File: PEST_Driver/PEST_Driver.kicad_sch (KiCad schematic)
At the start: 12 parts, among them J9 Conn_01x09, U1 INA199xxDCK

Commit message: Added independent signal ground to schematic
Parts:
- removed J9: Conn_01x09, Connector_PinSocket_2.54mm:PinSocket_1x09_P2.54mm_Vertical, symbol Connector_Generic:Conn_01x09
- added J9: Conn_01x10, symbol Connector_Generic:Conn_01x10
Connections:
- net CLK: now also J9.7 (Pin_7)
- net GND: now also J9.1 (Pin_1); no longer R100.2, R98.2, R99.2, U1.1 (REF), U1.2 (GND)
- net PWM: now also J9.9 (Pin_9)
- net RCLK: now also J9.8 (Pin_8)
- net SERX: now also J9.5 (Pin_5)
- net SERY: now also J9.6 (Pin_6)
- net VCC: now also J9.4 (Pin_4)
- net VIN: now also J9.2 (Pin_2)
- net VOUT: now also J9.10 (Pin_10)
- new net GNDS: J9.3 (Pin_3), R100.2, R98.2, R99.2, U1.1 (REF), U1.2 (GND)
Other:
- moved on the sheet: C19

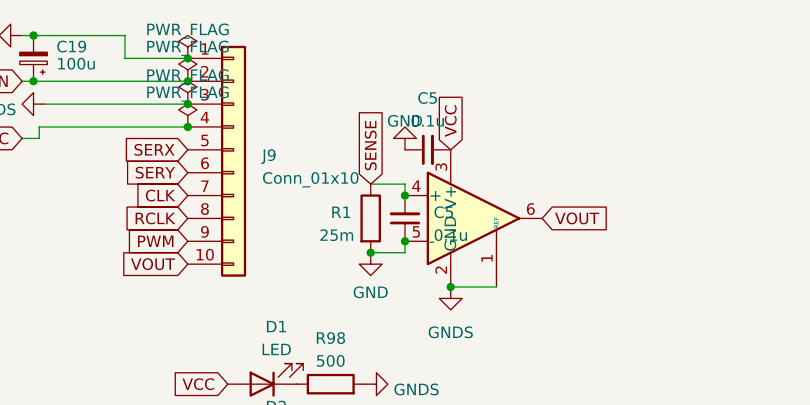
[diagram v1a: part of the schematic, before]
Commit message: Finished wiring independent MOSFET and logic grounds
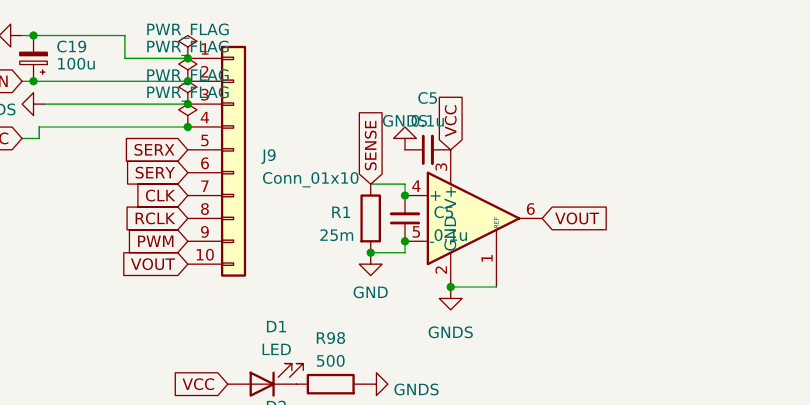
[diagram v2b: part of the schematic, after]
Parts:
- J9: footprint (none) -> Connector_PinSocket_2.54mm:PinSocket_1x10_P2.54mm_Vertical
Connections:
- net GND: no longer C5.1
- net GNDS: now also C5.1
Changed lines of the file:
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@@
-    )
-  )
-  (symbol (lib_id "power:GND") (at 60.325 28.575 180) (unit 1)
-    (in_bom yes) (on_board yes) (dnp no) (fields_autoplaced)
-    (property "Reference" "#PWR0126" (at 60.325 22.225 0)
-      (effects (font (size 1.27 1.27)) hide)
-    )
-    (property "Value" "GND" (at 60.325 25.4 0)
-      (effects (font (size 1.27 1.27)))
-    )
-    (property "Footprint" "" (at 60.325 28.575 0)
-      (effects (font (size 1.27 1.27)) hide)
-    )
-    (property "Datasheet" "" (at 60.325 28.575 0)
-      (effects (font (size 1.27 1.27)) hide)
-    )
-    (pin "1")
-    (instances
-      (project "PEST_Driver"
-        (path "/1312aa0a-e5d3-4b8d-ac4b-b6abdfb7d180/14e19459-9bf9-4345-8cad-a4f2aa65a7bc"
-          (reference "#PWR0126") (unit 1)
-        )
-        (path "/1312aa0a-e5d3-4b8d-ac4b-b6abdfb7d180"
-          (reference "#PWR0138") (unit 1)
-        )
-      )
     )
   )
@@
       (effects (font (size 1.27 1.27)) (justify left))
     )
-    (property "Footprint" "" (at 41.275 28.575 0)
+    (property "Footprint" "Connector_PinSocket_2.54mm:PinSocket_1x10_P2.54mm_Vertical" (at 41.275 28.575 0)
       (effects (font (size 1.27 1.27)) hide)
     )
@@
         )
       )
+    )
+  )
+  (symbol (lib_id "power:GNDS") (at 60.325 28.575 180) (unit 1)
+    (in_bom yes) (on_board yes) (dnp no) (fields_autoplaced)
+    (property "Reference" "#PWR078" (at 60.325 22.225 0)
+      (effects (font (size 1.27 1.27)) hide)
+    )
+    (property "Value" "GNDS" (at 60.325 25.4 0)
+      (effects (font (size 1.27 1.27)))
+    )
+    (property "Footprint" "" (at 60.325 28.575 0)
+      (effects (font (size 1.27 1.27)) hide)
+    )
+    (property "Datasheet" "" (at 60.325 28.575 0)
+      (effects (font (size 1.27 1.27)) hide)
+    )
+    (pin "1")
+    (instances
+      (project "PEST_Driver"
+        (path "/1312aa0a-e5d3-4b8d-ac4b-b6abdfb7d180"
+          (reference "#PWR078") (unit 1)
+        )
+      )

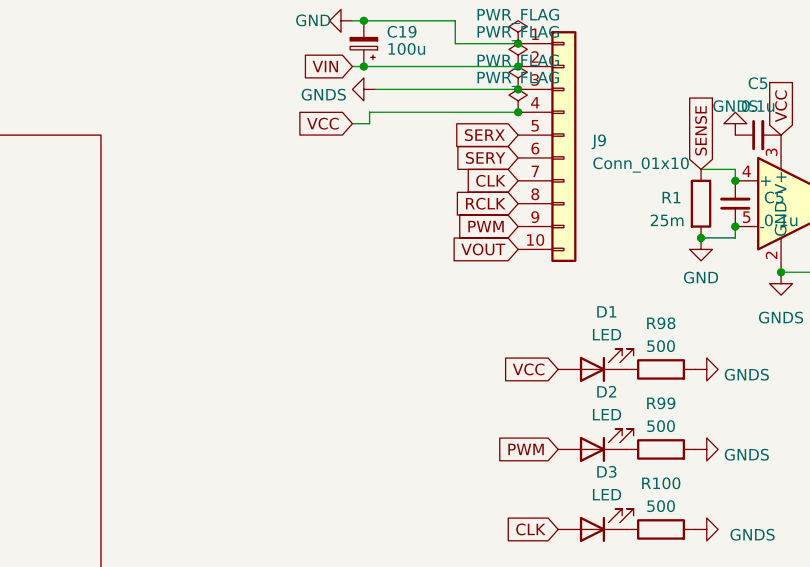
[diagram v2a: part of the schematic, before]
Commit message: Added more pulldown resistors to PEST Driver
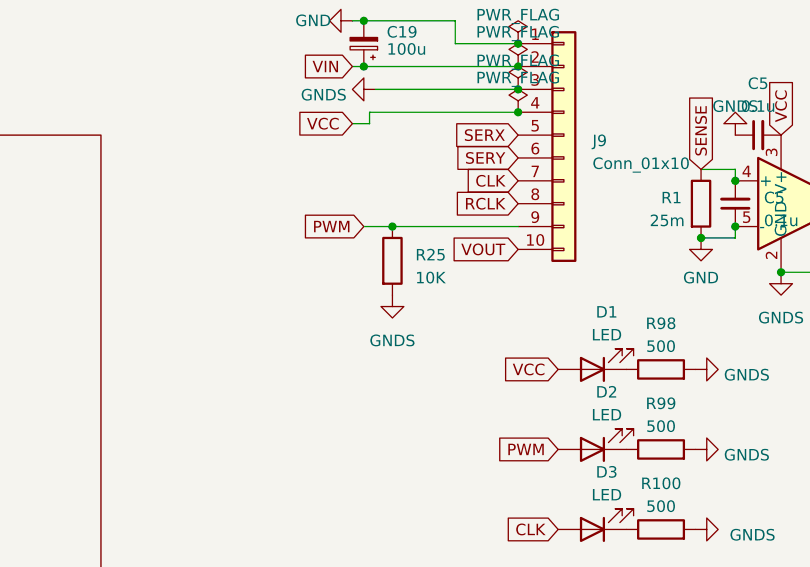
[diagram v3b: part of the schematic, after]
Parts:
- added R25: 10K, Resistor_SMD:R_0402_1005Metric, symbol Device:R
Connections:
- net GNDS: now also R25.2
- net PWM: now also R25.1
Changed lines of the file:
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@@
   (junction (at 56.515 40.005) (diameter 0) (color 0 0 0 0)
   )
+  (junction (at 22.225 38.735) (diameter 0) (color 0 0 0 0)
+  )
   (junction (at 60.325 33.655) (diameter 0) (color 0 0 0 0)
   )
@@
   (junction (at 19.05 15.875) (diameter 0) (color 0 0 0 0)
   )
+  (wire (pts (xy 22.225 38.735) (xy 36.195 38.735))
+    (stroke (width 0) (type default))
+  )
   (wire (pts (xy 65.405 43.815) (xy 70.485 43.815))
     (stroke (width 0) (type default))
@@
   )
   (wire (pts (xy 29.21 15.875) (xy 29.21 18.415))
+    (stroke (width 0) (type default))
+  )
+  (wire (pts (xy 19.05 38.735) (xy 22.225 38.735))
     (stroke (width 0) (type default))
   )
@@
     )
   )
-  (global_label "PWM" (shape input) (at 36.195 38.735 180) (fields_autoplaced)
-    (effects (font (size 1.27 1.27)) (justify right))
-    (property "Intersheetrefs" "${INTERSHEET_REFS}" (at 6.35 -6.35 0)
+  (global_label "PWM" (shape input) (at 19.05 38.735 180) (fields_autoplaced)
+    (effects (font (size 1.27 1.27)) (justify right))
+    (property "Intersheetrefs" "${INTERSHEET_REFS}" (at -10.795 -6.35 0)
       (effects (font (size 1.27 1.27)) hide)
     )
@@
     )
   )
+  (symbol (lib_id "Device:R") (at 22.225 42.545 0) (unit 1)
+    (in_bom yes) (on_board yes) (dnp no) (fields_autoplaced)
+    (property "Reference" "R25" (at 24.765 41.91 0)
+      (effects (font (size 1.27 1.27)) (justify left))
+    )
+    (property "Value" "10K" (at 24.765 44.45 0)
+      (effects (font (size 1.27 1.27)) (justify left))
+    )
+    (property "Footprint" "Resistor_SMD:R_0402_1005Metric" (at 20.447 42.545 90)
+      (effects (font (size 1.27 1.27)) hide)
+    )
+    (property "Datasheet" "~" (at 22.225 42.545 0)
+      (effects (font (size 1.27 1.27)) hide)
+    )
+    (pin "1")
+    (pin "2")
+    (instances
+      (project "PEST_Driver"
+        (path "/1312aa0a-e5d3-4b8d-ac4b-b6abdfb7d180/5f0c4818-2843-4085-a63a-fb9643216ecf"
+          (reference "R25") (unit 1)
+        )
+        (path "/1312aa0a-e5d3-4b8d-ac4b-b6abdfb7d180/14e19459-9bf9-4345-8cad-a4f2aa65a7bc"
+          (reference "R5") (unit 1)
+        )
+        (path "/1312aa0a-e5d3-4b8d-ac4b-b6abdfb7d180"
+          (reference "R66") (unit 1)
+        )
+      )
+    )
+  )
   (symbol (lib_id "Amplifier_Current:INA199xxDCK") (at 67.945 36.195 0) (unit 1)
     (in_bom yes) (on_board yes) (dnp no) (fields_autoplaced)
@@
         )
       )
+    )
+  )
+  (symbol (lib_id "power:GNDS") (at 22.225 46.355 0) (unit 1)
+    (in_bom yes) (on_board yes) (dnp no) (fields_autoplaced)
+    (property "Reference" "#PWR0111" (at 22.225 52.705 0)
+      (effects (font (size 1.27 1.27)) hide)
+    )
+    (property "Value" "GNDS" (at 22.225 51.435 0)
+      (effects (font (size 1.27 1.27)))
+    )
+    (property "Footprint" "" (at 22.225 46.355 0)
+      (effects (font (size 1.27 1.27)) hide)
+    )
+    (property "Datasheet" "" (at 22.225 46.355 0)
+      (effects (font (size 1.27 1.27)) hide)
+    )
+    (pin "1")
+    (instances
+      (project "PEST_Driver"
+        (path "/1312aa0a-e5d3-4b8d-ac4b-b6abdfb7d180"
+          (reference "#PWR0111") (unit 1)
+        )
+      )

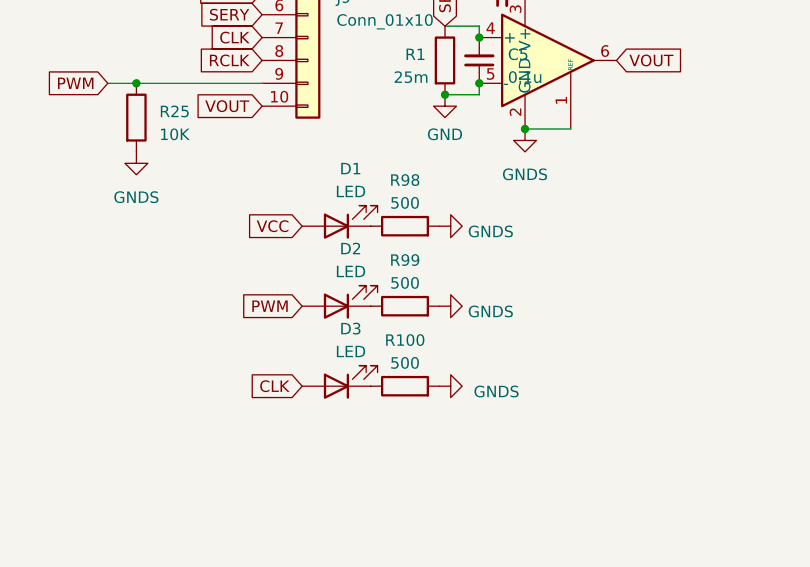
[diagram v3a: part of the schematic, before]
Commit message: Fixed some silkscreen stuff, started DRIFT bus layout
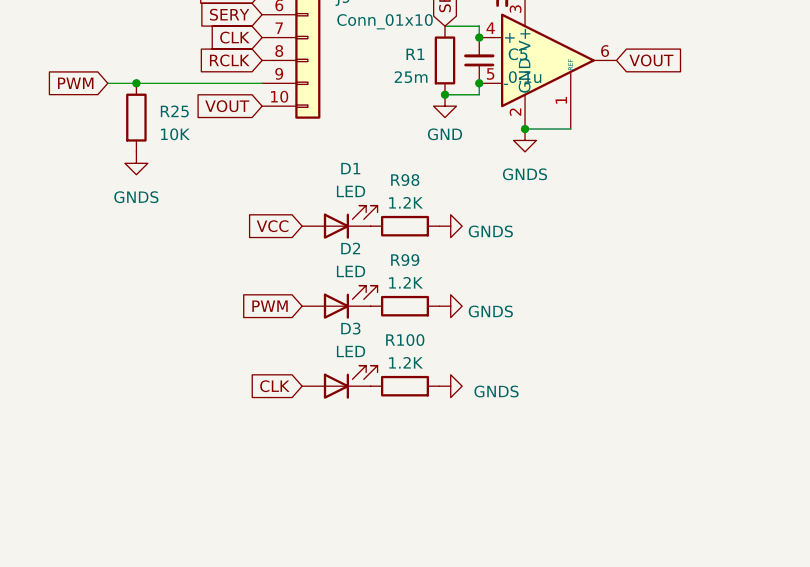
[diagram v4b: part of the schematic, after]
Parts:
- R100, R98, R99: value 500 -> 1.2K
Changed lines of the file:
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@@
       (effects (font (size 1.27 1.27)))
     )
-    (property "Value" "500" (at 52.07 60.96 90)
+    (property "Value" "1.2K" (at 52.07 60.96 90)
       (effects (font (size 1.27 1.27)))
     )
@@
       (effects (font (size 1.27 1.27)))
     )
-    (property "Value" "500" (at 52.07 69.85 90)
+    (property "Value" "1.2K" (at 52.07 69.85 90)
       (effects (font (size 1.27 1.27)))
     )
@@
       (effects (font (size 1.27 1.27)))
     )
-    (property "Value" "500" (at 52.07 52.07 90)
+    (property "Value" "1.2K" (at 52.07 52.07 90)
       (effects (font (size 1.27 1.27)))
     )
